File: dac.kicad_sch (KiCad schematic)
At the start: 17 parts, among them IC7 UDA1334BTS_N2,112

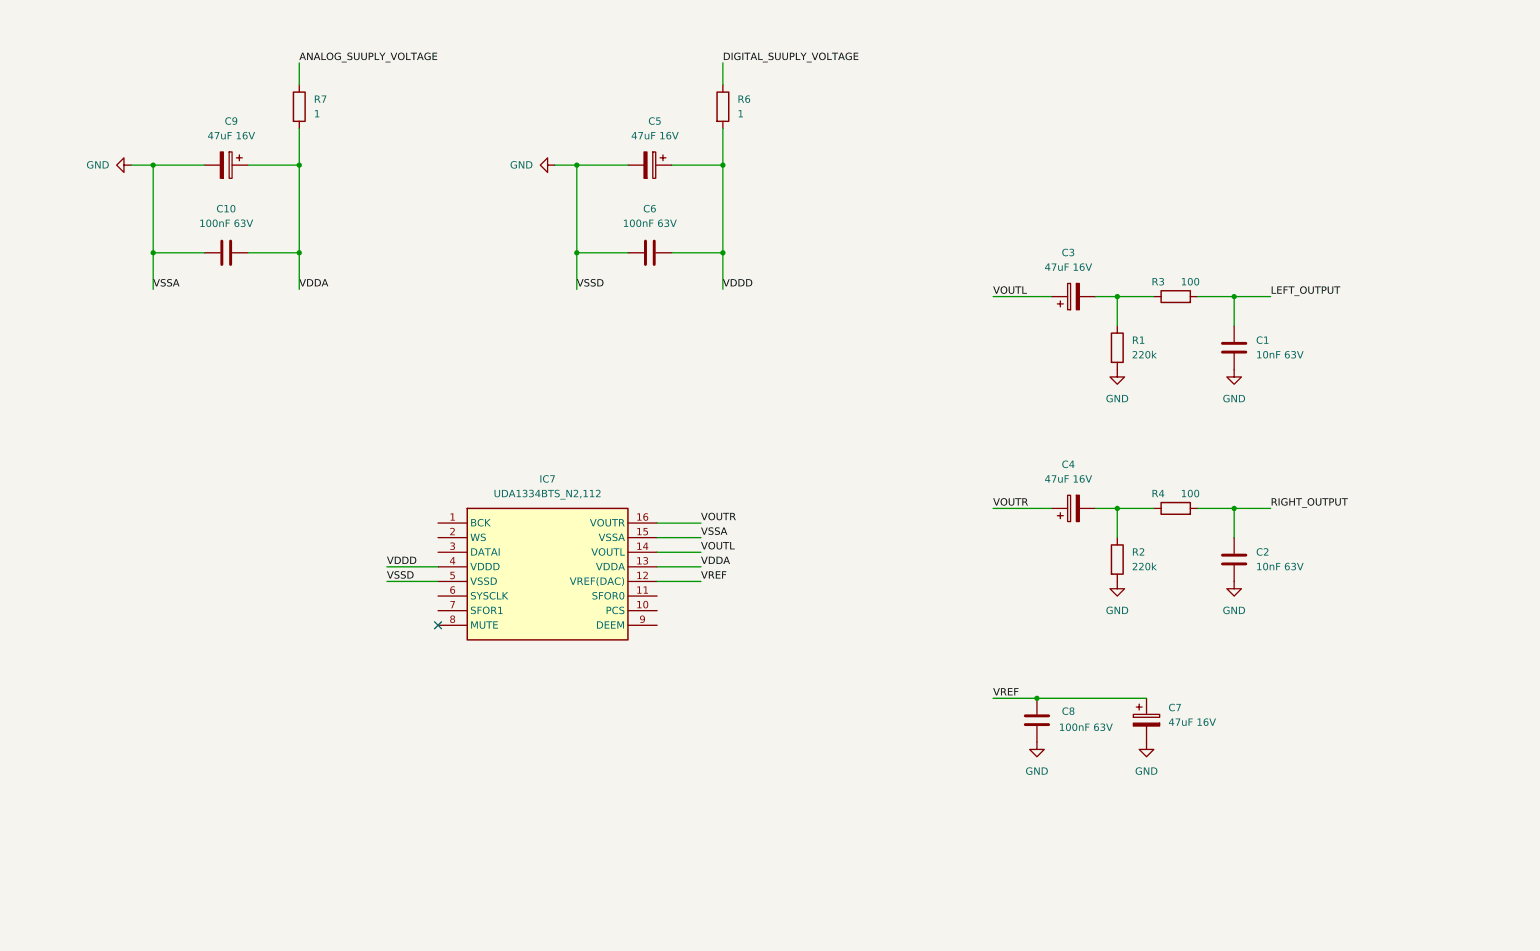
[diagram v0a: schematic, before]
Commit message: improve power delivery schema, improve dac, added oled, encoder, audio out
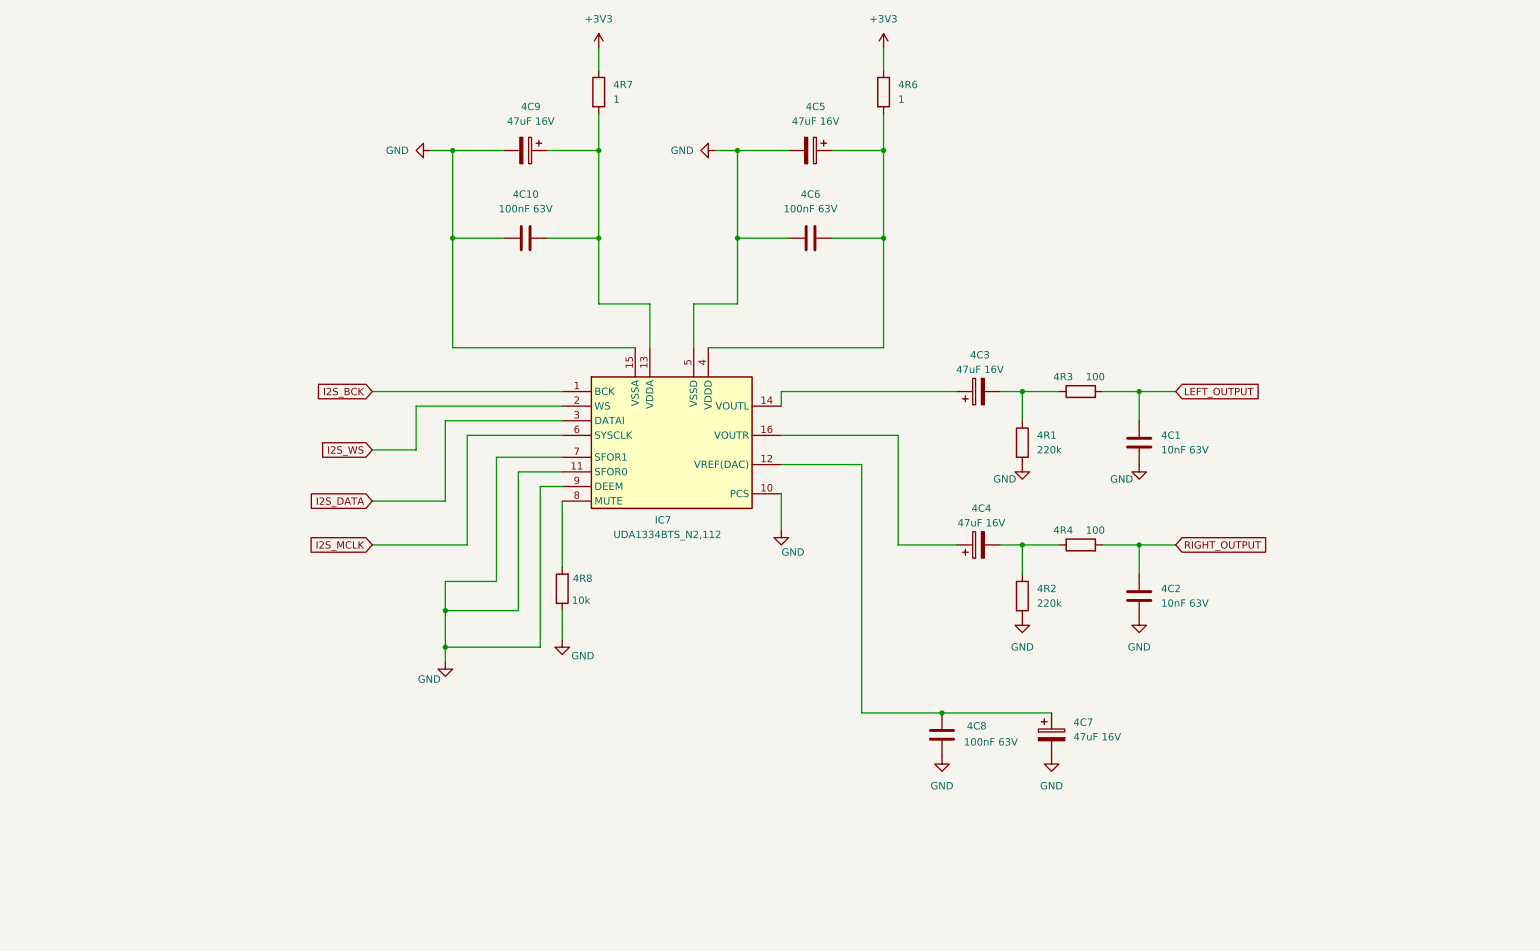
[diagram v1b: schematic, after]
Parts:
- added 4R8: 10k, symbol Device:R
- IC7: footprint SOP65P640X150-16N -> ipradio:SOP65P640X150-16N
- renumbered C1 to 4C1, C10 to 4C10, C2 to 4C2, C3 to 4C3, C4 to 4C4, C5 to 4C5, C6 to 4C6, C7 to 4C7, C8 to 4C8, C9 to 4C9, R1 to 4R1, R2 to 4R2, R3 to 4R3, R4 to 4R4, R6 to 4R6, R7 to 4R7
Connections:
- net DIGITAL_SUUPLY_VOLTAGE is gone; now on net +3V3: 4R6.1
- net GND: now also IC7.10 (PCS), IC7.11 (SFOR0), IC7.7 (SFOR1), IC7.9 (DEEM), 4R8.1
- net I2S_BCK: now reaches IC7.1 (BCK)
- net I2S_WS: now reaches IC7.2 (WS)
- net I2S_DATA: now reaches IC7.3 (DATAI)
- net I2S_MCLK: now reaches IC7.6 (SYSCLK)
- net at IC7.8 (MUTE): now also 4R8.2
- net ANALOG_SUUPLY_VOLTAGE renamed +3V3
- net VDDA: no longer names the net of 4C10.1, 4C9.1, 4R7.2, IC7.13 (VDDA)
- net VDDD: no longer names the net of 4C5.1, 4C6.1, 4R6.2, IC7.4 (VDDD)
- net VOUTL: no longer names the net of 4C3.1, IC7.14 (VOUTL)
- net VOUTR: no longer names the net of 4C4.1, IC7.16 (VOUTR)
- net VREF: no longer names the net of 4C7.1, 4C8.1, IC7.12 (VREF(DAC))
- no-connect marks 1 -> 0
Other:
- moved on the sheet: 4C1, 4C10, 4C2, 4C3, 4C4, 4C5, 4C6, 4C7, 4C8, 4C9, 4R1, 4R2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

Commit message: finalize power and esp schemas
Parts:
- 4C1, 4C10, 4C2, 4C6, 4C8: footprint (none) -> Capacitor_SMD:C_0402_1005Metric
- 4C3, 4C4, 4C5, 4C7, 4C9: footprint (none) -> Capacitor_Tantalum_SMD:CP_EIA-3528-21_Kemet-B
- 4R1, 4R2, 4R3, 4R4, 4R6, 4R7, 4R8: footprint (none) -> Resistor_SMD:R_0402_1005Metric
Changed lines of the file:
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@@
 			)
 		)
-		(property "Footprint" ""
+		(property "Footprint" "Capacitor_Tantalum_SMD:CP_EIA-3528-21_Kemet-B"
 			(at 99.06 41.6052 0)
 			(hide yes)
@@
 			)
 		)
-		(property "Footprint" ""
+		(property "Footprint" "Capacitor_SMD:C_0402_1005Metric"
 			(at 99.06 56.8452 0)
 			(hide yes)
@@
 			)
 		)
-		(property "Footprint" ""
+		(property "Footprint" "Capacitor_Tantalum_SMD:CP_EIA-3528-21_Kemet-B"
 			(at 148.59 41.6052 0)
 			(hide yes)
@@
 			)
 		)
-		(property "Footprint" ""
+		(property "Footprint" "Capacitor_SMD:C_0402_1005Metric"
 			(at 176.2252 146.05 0)
 			(hide yes)
@@
 			)
 		)
-		(property "Footprint" ""
+		(property "Footprint" "Resistor_SMD:R_0402_1005Metric"
 			(at 199.39 84.328 90)
 			(hide yes)
@@
 			)
 		)
-		(property "Footprint" ""
+		(property "Footprint" "Capacitor_Tantalum_SMD:CP_EIA-3528-21_Kemet-B"
 			(at 185.42 81.5848 0)
 			(hide yes)
@@
 			)
 		)
-		(property "Footprint" ""
+		(property "Footprint" "Resistor_SMD:R_0402_1005Metric"
 			(at 187.452 91.44 90)
 			(hide yes)
@@
 			)
 		)
-		(property "Footprint" ""
+		(property "Footprint" "Resistor_SMD:R_0402_1005Metric"
 			(at 199.39 110.998 90)
 			(hide yes)
@@
 			)
 		)
-		(property "Footprint" ""
+		(property "Footprint" "Resistor_SMD:R_0402_1005Metric"
 			(at 110.998 116.84 90)
 			(hide yes)
@@
 			)
 		)
-		(property "Footprint" ""
+		(property "Footprint" "Resistor_SMD:R_0402_1005Metric"
 			(at 187.452 118.11 90)
 			(hide yes)
@@
 			)
 		)
-		(property "Footprint" ""
+		(property "Footprint" "Capacitor_SMD:C_0402_1005Metric"
 			(at 210.5152 95.25 0)
 			(hide yes)
@@
 			)
 		)
-		(property "Footprint" ""
+		(property "Footprint" "Capacitor_Tantalum_SMD:CP_EIA-3528-21_Kemet-B"
 			(at 195.2752 146.05 0)
 			(hide yes)
@@
 			)
 		)
-		(property "Footprint" ""
+		(property "Footprint" "Capacitor_Tantalum_SMD:CP_EIA-3528-21_Kemet-B"
 			(at 185.42 108.2548 0)
 			(hide yes)
@@
 			)
 		)
-		(property "Footprint" ""
+		(property "Footprint" "Resistor_SMD:R_0402_1005Metric"
 			(at 113.792 30.48 90)
 			(hide yes)
@@
 			)
 		)
-		(property "Footprint" ""
+		(property "Footprint" "Capacitor_SMD:C_0402_1005Metric"
 			(at 148.59 56.8452 0)
 			(hide yes)
@@
 			)
 		)
-		(property "Footprint" ""
+		(property "Footprint" "Resistor_SMD:R_0402_1005Metric"
 			(at 163.322 30.48 90)
 			(hide yes)
@@
 			)
 		)
-		(property "Footprint" ""
+		(property "Footprint" "Capacitor_SMD:C_0402_1005Metric"
 			(at 210.5152 121.92 0)
 			(hide yes)

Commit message: finalized schema
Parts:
- added 4C11: 1uF, Capacitor_SMD:C_0402_1005Metric, symbol Device:C
- added 4C12, 4C13: 100nF, Capacitor_SMD:C_0402_1005Metric, symbol Device:C
- added 4FB1: 100mHz, Inductor_SMD:L_0402_1005Metric, symbol Device:FerriteBead
- added 4R10, 4R11, 4R9: 10k, Resistor_SMD:R_0402_1005Metric, symbol Device:R
- added 4R5: 5.1k, Resistor_SMD:R_0402_1005Metric, symbol Device:R
- added IC5: NJM2882F33-TE1, ipradio:SOT95P280X130-5N, symbol ipradio:NJM2882F33-TE1
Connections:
- net +3V3: no longer 4R7.1
- net GND: no longer 4C1.2, 4C10.2, 4C2.2, 4C7.2, 4C8.2, 4C9.2, 4R1.2, 4R2.2, 4R8.1, IC7.10 (PCS), IC7.11 (SFOR0), IC7.15 (VSSA), IC7.7 (SFOR1), IC7.9 (DEEM)
- net I2S_MCLK: no longer names the net of IC7.6 (SYSCLK)
- new net: 4R9.2, IC7.9 (DEEM)
- new net: 4C13.1, IC5.4 (NOISE_BYPASS)
- new net: 4C11.1, 4C12.1, 4FB1.1, 4R5.1, IC5.1 (VIN)
- new net: 4R10.2, IC7.11 (SFOR0)
- new net: 4R11.2, IC7.7 (SFOR1)
- new net: 4R5.2, IC5.3 (CONTROL_(ACTIVE_HIGH))
- new net GNDA: 4C1.2, 4C10.2, 4C11.2, 4C12.2, 4C13.2, 4C2.2, 4C7.2, 4C8.2, 4C9.2, 4R1.2, 4R10.1, 4R11.1, 4R2.2, 4R8.1, 4R9.1, IC5.2 (GND), IC7.15 (VSSA)
- new net VDDA3V3: 4R7.1, IC5.5 (VOUT)
- new net V_SYS_5V2A: 4FB1.2
- no-connect marks 0 -> 2
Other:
- moved on the sheet: 4C1, 4C10, 4C2, 4C3, 4C4, 4C5, 4C6, 4C7, 4C8, 4C9, 4R1, 4R2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
